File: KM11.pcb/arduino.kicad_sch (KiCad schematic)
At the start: 15 parts, among them J10 ARDUINO POWER, J11 AUX, J9 UART1_RS232_Schneid-Klemm_2x5, SW1 Option, SW2 Reset, U1 MAX232

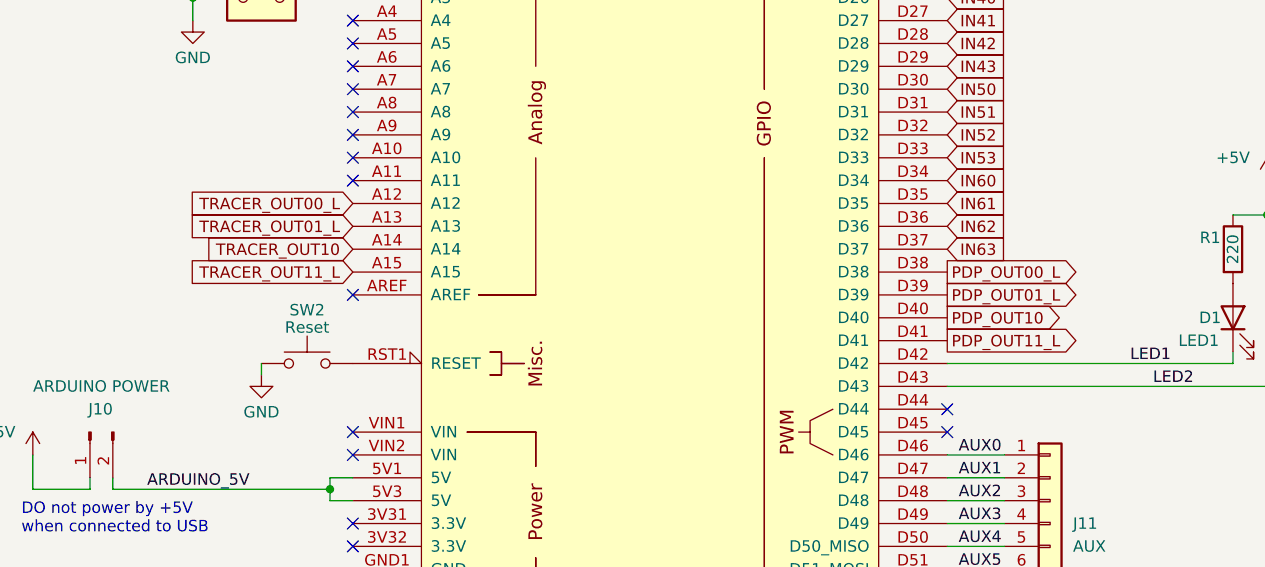
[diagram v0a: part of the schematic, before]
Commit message: Fix of KM11 wiring out01 <-> out10
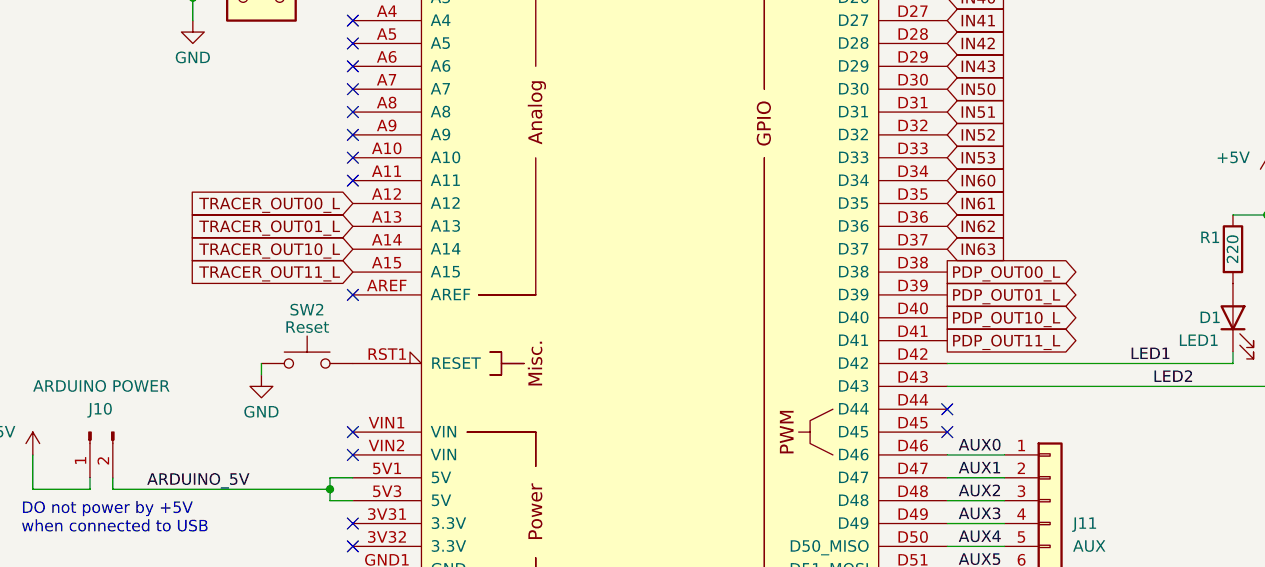
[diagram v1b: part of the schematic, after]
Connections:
- net PDP_OUT10 renamed PDP_OUT10_L
- net TRACER_OUT10 renamed TRACER_OUT10_L

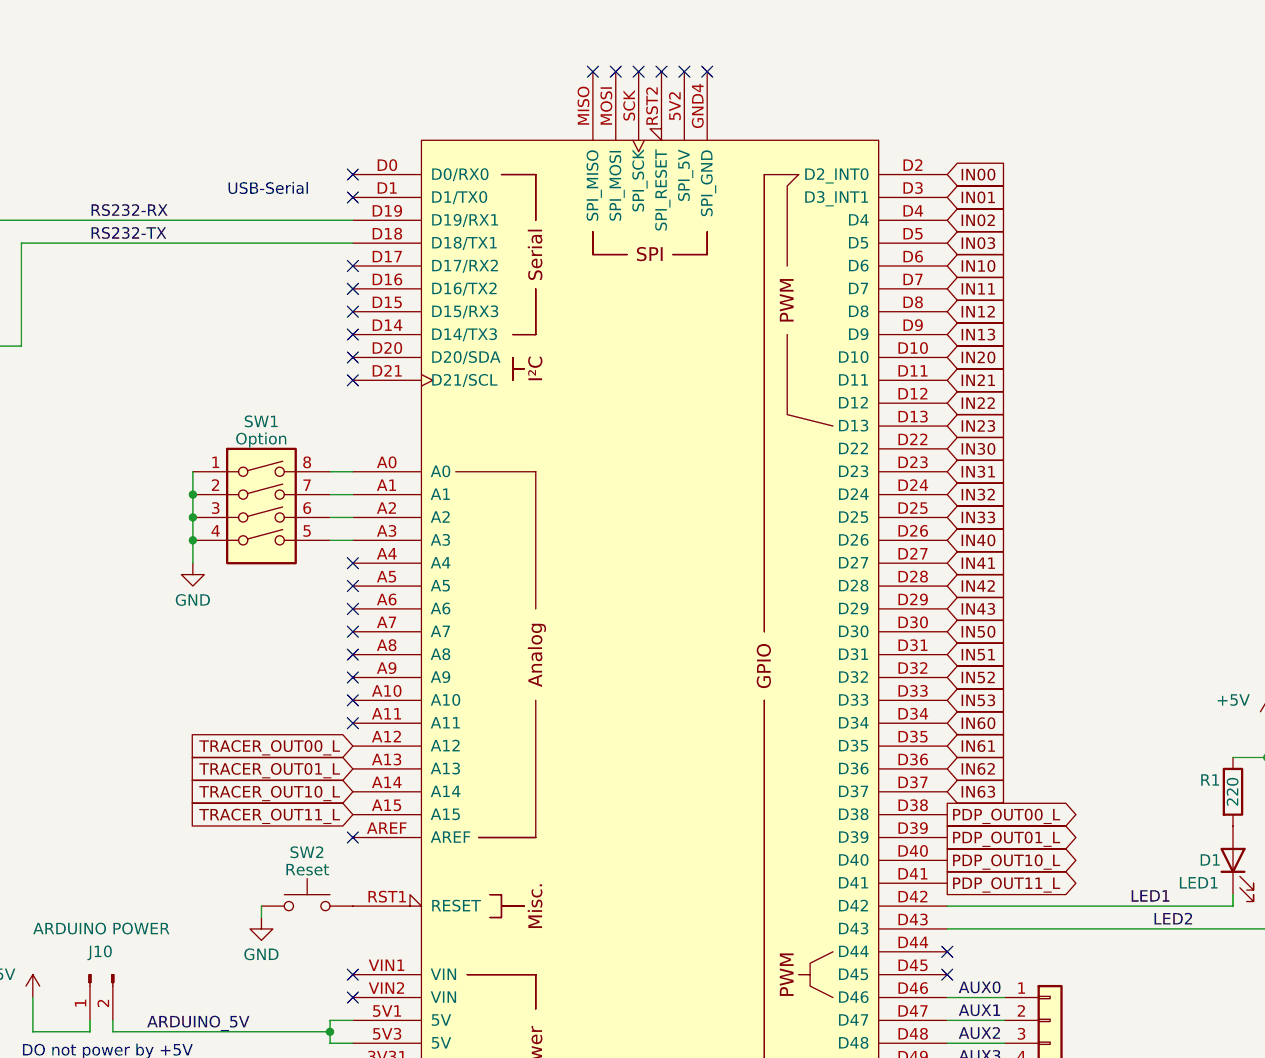
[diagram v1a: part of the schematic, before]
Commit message: ^repalce synthetic KM11 signals "Inxx, out**" with flipchip pin names
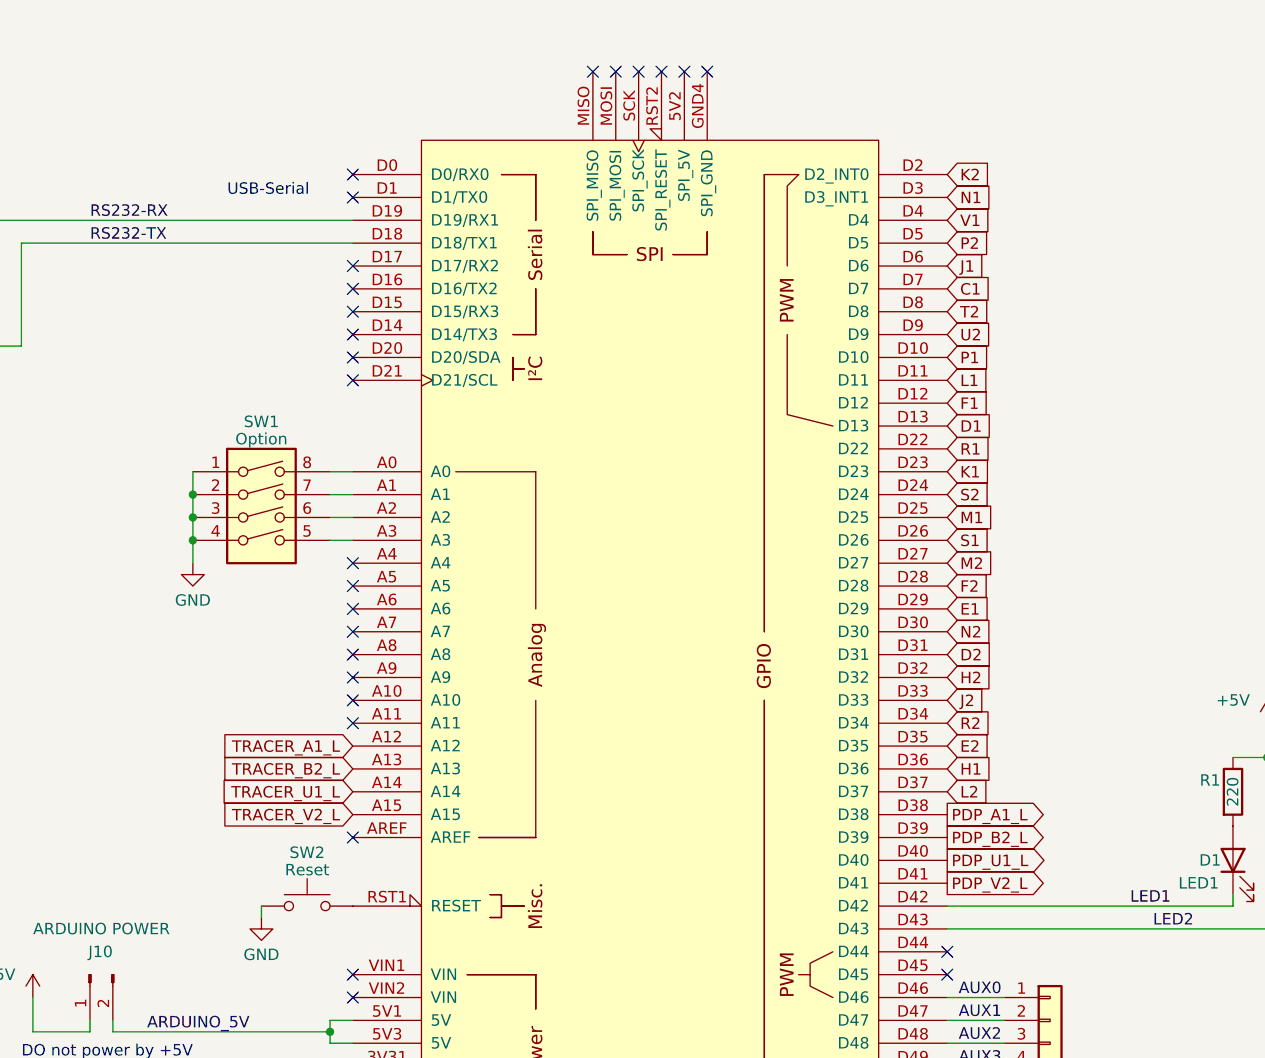
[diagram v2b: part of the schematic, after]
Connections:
- net IN00 renamed K2
- net IN01 renamed N1
- net IN02 renamed V1
- net IN03 renamed P2
- net IN10 renamed J1
- net IN11 renamed C1
- net IN12 renamed T2
- net IN13 renamed U2
- net IN20 renamed P1
- net IN21 renamed L1
- net IN22 renamed F1
- net IN23 renamed D1
- net IN30 renamed R1
- net IN31 renamed K1
- net IN32 renamed S2
- net IN33 renamed M1
- net IN40 renamed S1
- net IN41 renamed M2
- net IN42 renamed F2
- net IN43 renamed E1
- net IN50 renamed N2
- net IN51 renamed D2
- net IN52 renamed H2
- net IN53 renamed J2
- net IN60 renamed R2
- net IN61 renamed E2
- net IN62 renamed H1
- net IN63 renamed L2
- net PDP_OUT00_L renamed PDP_A1_L
- net PDP_OUT01_L renamed PDP_B2_L
- net PDP_OUT10_L renamed PDP_U1_L
- net PDP_OUT11_L renamed PDP_V2_L
- net TRACER_OUT00_L renamed TRACER_A1_L
- net TRACER_OUT01_L renamed TRACER_B2_L
- net TRACER_OUT10_L renamed TRACER_U1_L
- net TRACER_OUT11_L renamed TRACER_V2_L
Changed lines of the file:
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@@
 		)
 	)
-	(global_label "IN40"
+	(global_label "S1"
 		(shape input)
 		(at 226.06 83.82 0)
@@
 		)
 	)
-	(global_label "IN13"
+	(global_label "U2"
 		(shape input)
 		(at 226.06 60.96 0)
@@
 		)
 	)
-	(global_label "TRACER_OUT10_L"
+	(global_label "TRACER_U1_L"
 		(shape input)
 		(at 160.02 111.76 180)
@@
 		)
 	)
-	(global_label "IN03"
+	(global_label "P2"
 		(shape input)
 		(at 226.06 50.8 0)
@@
 		)
 	)
-	(global_label "PDP_OUT01_L"
+	(global_label "PDP_B2_L"
 		(shape output)
 		(at 226.06 116.84 0)
@@
 		)
 	)
-	(global_label "IN61"
+	(global_label "E2"
 		(shape input)
 		(at 226.06 106.68 0)
@@
 		)
 	)
-	(global_label "PDP_OUT10_L"
+	(global_label "PDP_U1_L"
 		(shape output)
 		(at 226.06 119.38 0)
@@
 		)
 	)
-	(global_label "IN23"
+	(global_label "D1"
 		(shape input)
 		(at 226.06 71.12 0)
@@
 		)
 	)
-	(global_label "IN52"
+	(global_label "H2"
 		(shape input)
 		(at 226.06 99.06 0)
@@
 		)
 	)
-	(global_label "TRACER_OUT00_L"
+	(global_label "TRACER_A1_L"
 		(shape input)
 		(at 160.02 106.68 180)
@@
 		)
 	)
-	(global_label "IN12"
+	(global_label "T2"
 		(shape input)
 		(at 226.06 58.42 0)
@@
 		)
 	)
-	(global_label "IN62"
+	(global_label "H1"
 		(shape input)
 		(at 226.06 109.22 0)
@@
 		)
 	)
-	(global_label "IN00"
+	(global_label "K2"
 		(shape input)
 		(at 226.06 43.18 0)
@@
 		)
 	)
-	(global_label "IN60"
+	(global_label "R2"
 		(shape input)
 		(at 226.06 104.14 0)
@@
 		)
 	)
-	(global_label "PDP_OUT00_L"
+	(global_label "PDP_A1_L"
 		(shape output)
 		(at 226.06 114.3 0)
@@
 		)
 	)
-	(global_label "IN21"
+	(global_label "L1"
 		(shape input)
 		(at 226.06 66.04 0)
@@
 		)
 	)
-	(global_label "IN42"
+	(global_label "F2"
 		(shape input)
 		(at 226.06 88.9 0)
@@
 		)
 	)
-	(global_label "IN43"
+	(global_label "E1"
 		(shape input)
 		(at 226.06 91.44 0)
@@
 		)
 	)
-	(global_label "IN30"
+	(global_label "R1"
 		(shape input)
 		(at 226.06 73.66 0)
@@
 		)
 	)
-	(global_label "IN01"
+	(global_label "N1"
 		(shape input)
 		(at 226.06 45.72 0)
@@
 		)
 	)
-	(global_label "IN51"
+	(global_label "D2"
 		(shape input)
 		(at 226.06 96.52 0)
@@
 		)
 	)
-	(global_label "IN32"
+	(global_label "S2"
 		(shape input)
 		(at 226.06 78.74 0)
@@
 		)
 	)
-	(global_label "IN10"
+	(global_label "J1"
 		(shape input)
 		(at 226.06 53.34 0)
@@
 		)
 	)
-	(global_label "IN31"
+	(global_label "K1"
 		(shape input)
 		(at 226.06 76.2 0)
@@
 		)
 	)
-	(global_label "IN20"
+	(global_label "P1"
 		(shape input)
 		(at 226.06 63.5 0)
@@
 		)
 	)
-	(global_label "IN41"
+	(global_label "M2"
 		(shape input)
 		(at 226.06 86.36 0)
@@
 		)
 	)
-	(global_label "IN02"
+	(global_label "V1"
 		(shape input)
 		(at 226.06 48.26 0)
@@
 		)
 	)
-	(global_label "PDP_OUT11_L"
+	(global_label "PDP_V2_L"
 		(shape output)
 		(at 226.06 121.92 0)
@@
 		)
 	)
-	(global_label "IN50"
+	(global_label "N2"
 		(shape input)
 		(at 226.06 93.98 0)
@@
 		)
 	)
-	(global_label "IN22"
+	(global_label "F1"
 		(shape input)
 		(at 226.06 68.58 0)
@@
 		)
 	)
-	(global_label "TRACER_OUT11_L"
+	(global_label "TRACER_V2_L"
 		(shape input)
 		(at 160.02 114.3 180)
@@
 		)
 	)
-	(global_label "IN33"
+	(global_label "M1"
 		(shape input)
 		(at 226.06 81.28 0)
@@
 		)
 	)
-	(global_label "IN11"
+	(global_label "C1"
 		(shape input)
 		(at 226.06 55.88 0)
@@
 		)
 	)
-	(global_label "IN53"
+	(global_label "J2"
 		(shape input)
 		(at 226.06 101.6 0)
@@
 		)
 	)
-	(global_label "TRACER_OUT01_L"
+	(global_label "TRACER_B2_L"
 		(shape input)
 		(at 160.02 109.22 180)
@@
 		)
 	)
-	(global_label "IN63"
+	(global_label "L2"
 		(shape input)
 		(at 226.06 111.76 0)
@@
 	)
 	(symbol
+		(lib_name "GND_4")
 		(lib_id "power:GND")
 		(at 157.48 151.13 0)
@@
 			)
 		)
-		(property "Description" ""
+		(property "Description" "Power symbol creates a global label with name \"GND\" , ground"
 			(at 157.48 151.13 0)
 			(effects
@@
 			)
 		)
-		(property "Description" ""
+		(property "Description" "Power symbol creates a global label with name \"GND\" , ground"
 			(at 142.24 86.36 0)
 			(effects
@@
 	)
 	(symbol
+		(lib_name "+5V_2")
 		(lib_id "power:+5V")
 		(at 124.46 134.62 0)
@@
 			)
 		)
-		(property "Description" ""
+		(property "Description" "Power symbol creates a global label with name \"+5V\""
 			(at 124.46 134.62 0)
 			(effects
@@
 	)
 	(symbol
+		(lib_name "GND_2")
 		(lib_id "power:GND")
 		(at 48.26 76.2 0)
@@
 			)
 		)
-		(property "Description" ""
+		(property "Description" "Power symbol creates a global label with name \"GND\" , ground"
 			(at 48.26 76.2 0)
 			(effects
@@
 	)
 	(symbol
+		(lib_name "GND_1")
 		(lib_id "power:GND")
 		(at 93.98 90.17 0)
@@
 			)
 		)
-		(property "Description" ""
+		(property "Description" "Power symbol creates a global label with name \"GND\" , ground"
 			(at 93.98 90.17 0)
 			(effects
@@
 	)
 	(symbol
+		(lib_name "GND_3")
 		(lib_id "power:GND")
 		(at 62.23 57.15 0)
@@
 			)
 		)
-		(property "Description" ""
+		(property "Description" "Power symbol creates a global label with name \"GND\" , ground"
 			(at 62.23 57.15 0)
 			(effects
@@
 	)
 	(symbol
+		(lib_name "+5V_1")
 		(lib_id "power:+5V")
 		(at 93.98 29.21 0)
@@
 			)
 		)
-		(property "Description" ""
+		(property "Description" "Power symbol creates a global label with name \"+5V\""
 			(at 93.98 29.21 0)
 			(effects
@@
 	)
 	(symbol
+		(lib_name "GND_5")
 		(lib_id "power:GND")
 		(at 149.86 125.73 0)
@@
 			)
 		)
-		(property "Description" ""
+		(property "Description" "Power symbol creates a global label with name \"GND\" , ground"
 			(at 149.86 125.73 0)
 			(effects
@@
 			)
 		)
-		(property "Description" ""
+		(property "Description" "Power symbol creates a global label with name \"+5V\""
 			(at 261.62 104.14 0)
 			(effects
